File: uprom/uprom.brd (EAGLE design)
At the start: 30.5 x 48.3 mm, 10 parts, among them IC1 27C128P, T1 2N3904, T2 2N3904

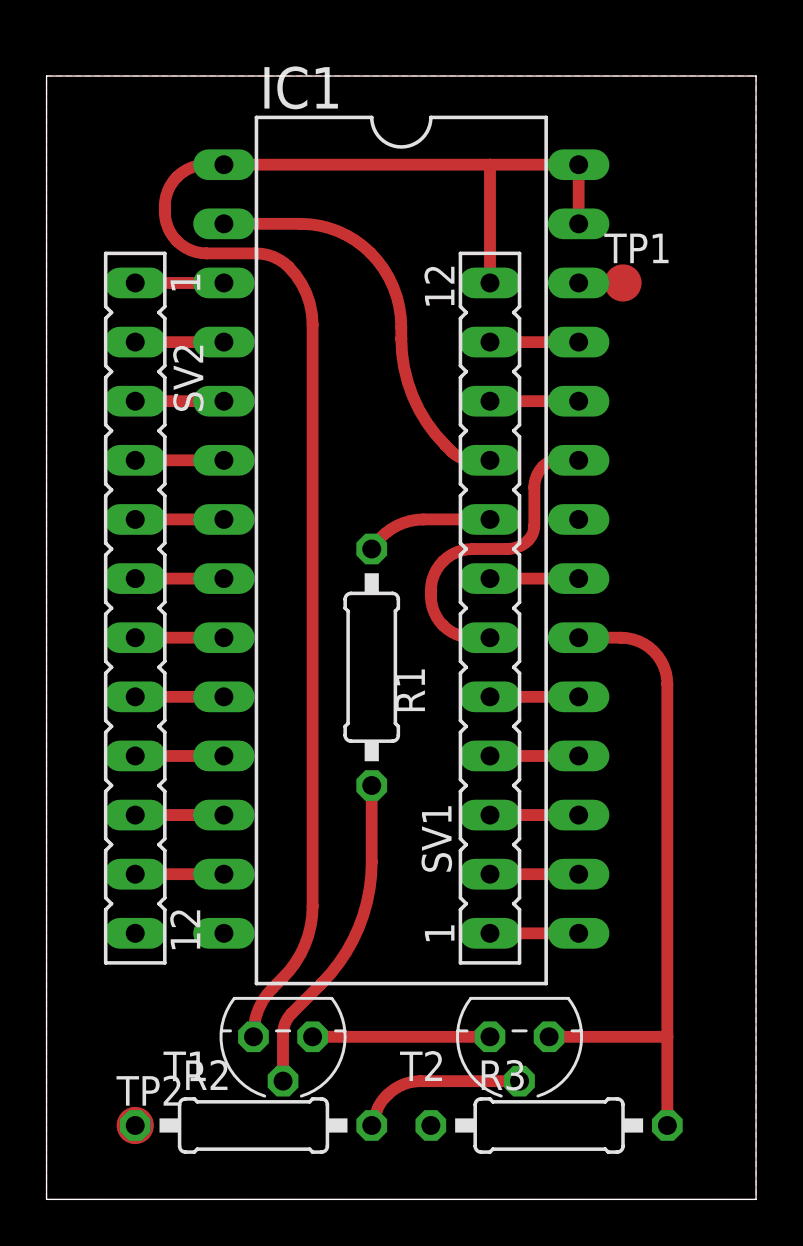
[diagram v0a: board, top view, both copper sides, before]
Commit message: compact sizr
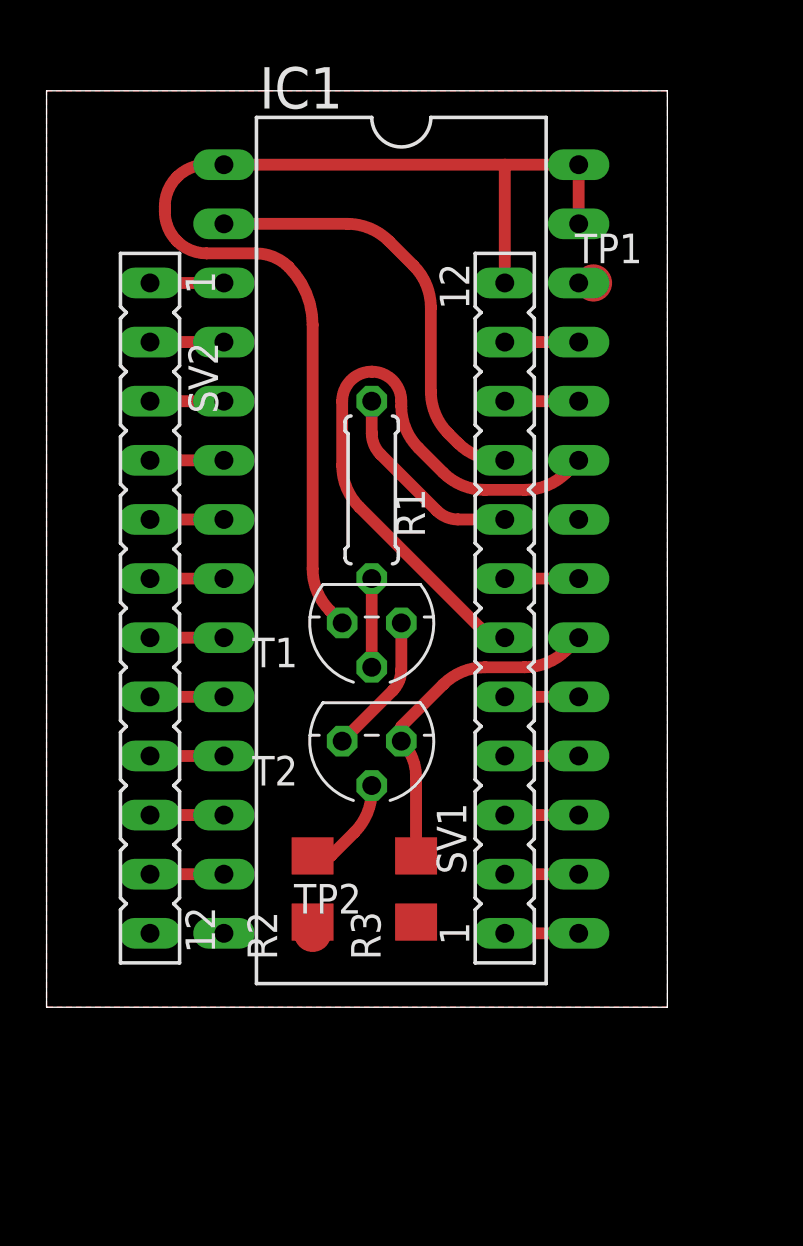
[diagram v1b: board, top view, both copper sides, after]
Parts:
- R1: device rcl:0207/10 -> rcl:0207/7
- R2, R3: device rcl:0207/10 -> rcl:R1206
- moved T1 18.2 mm to (12.7, 24.8)
- moved T2 14.2 mm to (12.7, 19.7)
- moved R3 11.7 mm to (14.6, 13.3), turned to 90 degrees
- moved TP2 11.2 mm to (10.2, 11.4)
- moved R2 10.5 mm to (10.2, 13.3), turned to 90 degrees
- moved R1 7.62 mm to (12.7, 30.5)
- moved TP1 1.27 mm to (22.2, 39.4)
- moved SV2 0.63 mm to (3.17, 25.4)
- moved SV1 0.63 mm to (18.4, 25.4)
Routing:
- net VCC: track 66.8 -> 48.8 mm
- net !CS: track 28.7 -> 14.6 mm
- net A11: track 13.8 -> 26.7 mm
- net N$1: track 13.7 -> 3.81 mm
- net !SEL_F_C: track 5.45 -> 8.77 mm
- net N$2: track 7.29 -> 4.38 mm
- net N$3: track 7.62 -> 6.05 mm
- net A12: track 17.6 -> 19.0 mm
- net A13: track 1.91 -> 0.64 mm
- net D2: track 3.81 -> 3.17 mm
- net D1: track 3.81 -> 3.17 mm
- net D0: track 3.81 -> 3.17 mm
- net A7: track 3.81 -> 3.17 mm
- net A6: track 3.81 -> 3.17 mm
- net A5: track 3.81 -> 3.17 mm
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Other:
- board size 30.5 x 48.3 mm -> 26.7 x 39.4 mm
